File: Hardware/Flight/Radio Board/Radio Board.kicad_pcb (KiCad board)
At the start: 2 copper layers, 82 x 82 mm, 16 parts, among them J1 Conn_01x20_Female, J2 Conn_Coaxial, J3 Conn_Coaxial, U1 RFM95W-915S2, U2 RFM95W-915S2

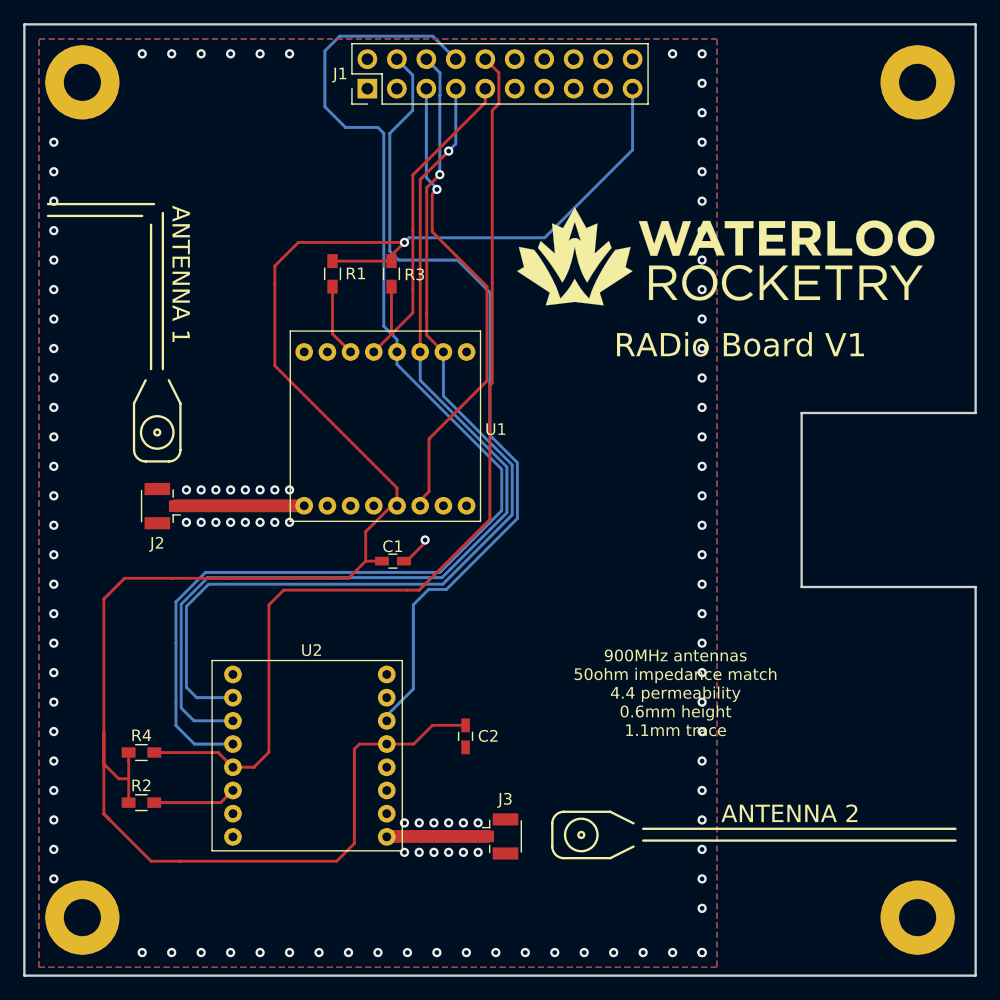
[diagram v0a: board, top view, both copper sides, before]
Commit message: Radio Review
Added Debug LEDs
Rerouted traces to keep away from edge
Made RF traces shorter
Switched RFM95W to SMD version
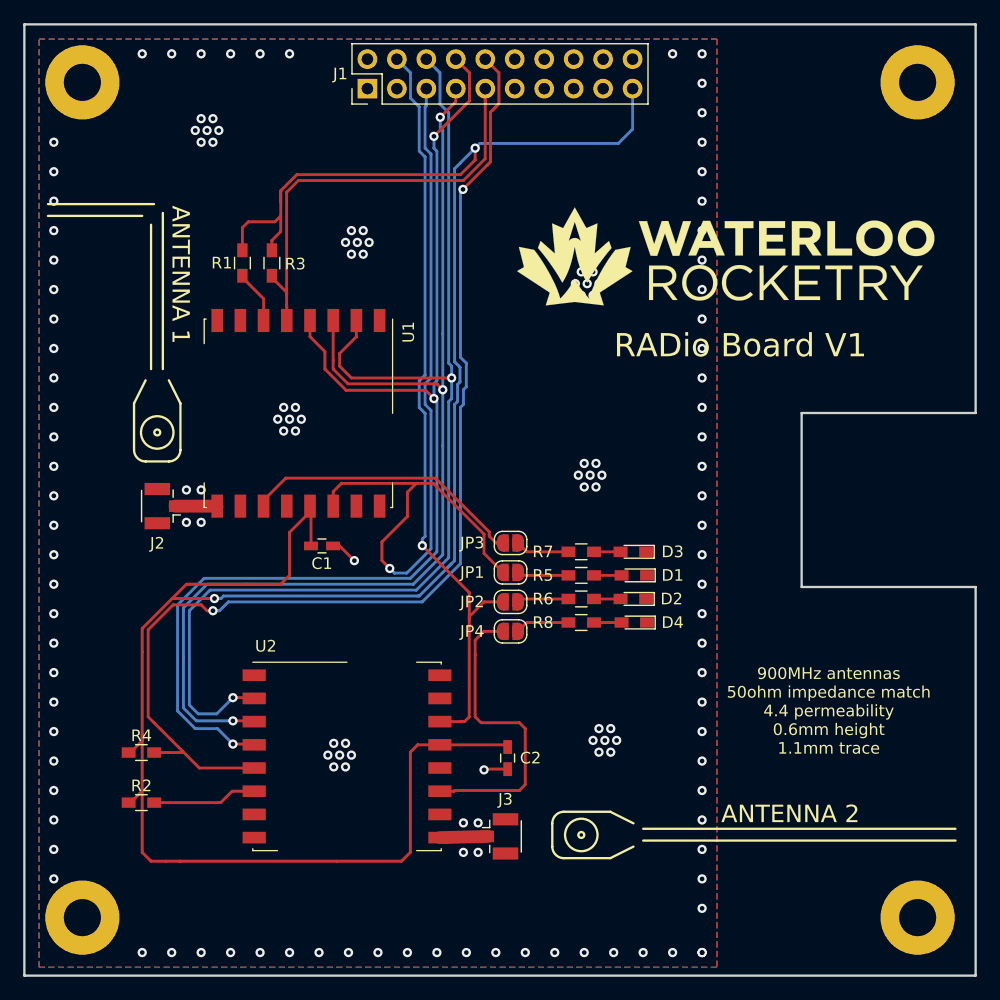
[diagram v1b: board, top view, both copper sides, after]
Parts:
- added D1: LED, LEDs:LED_0603_HandSoldering, F.Cu at (52.6, 47.5)
- added D2: LED, LEDs:LED_0603_HandSoldering, F.Cu at (52.5, 49.5)
- added D3: LED, LEDs:LED_0603_HandSoldering, F.Cu at (52.5, 45.5)
- added D4: LED, LEDs:LED_0603_HandSoldering, F.Cu at (52.6, 51.6)
- added JP1: Jumper, Jumper:SolderJumper-2_P1.3mm_Open_RoundedPad1.0x1.5mm, F.Cu at (41.9, 47.2)
- added JP2: Jumper, Jumper:SolderJumper-2_P1.3mm_Open_RoundedPad1.0x1.5mm, F.Cu at (41.9, 49.8)
- added JP3: Jumper, Jumper:SolderJumper-2_P1.3mm_Open_RoundedPad1.0x1.5mm, F.Cu at (41.9, 44.7)
- added JP4: Jumper, Jumper:SolderJumper-2_P1.3mm_Open_RoundedPad1.0x1.5mm, F.Cu at (41.9, 52.3)
- added R5: 70, Resistors_SMD:R_0603_HandSoldering, F.Cu at (48.0, 47.5)
- added R6: 70, Resistors_SMD:R_0603_HandSoldering, F.Cu at (48.0, 49.5)
- added R7: 70, Resistors_SMD:R_0603_HandSoldering, F.Cu at (48.0, 45.5)
- added R8: 70, Resistors_SMD:R_0603_HandSoldering, F.Cu at (48.0, 51.6)
- U1, U2: footprint Payload_Radios:Hopref_RFM9XW_THT -> RF_Modules:Hopref_RFM9XW_SMD
- moved U1 15.4 mm to (23.6, 33.5)
- moved U2 12.1 mm to (27.8, 63.1)
- moved R3 10.4 mm to (21.3, 20.6)
- moved R1 7.82 mm to (18.8, 20.6)
- moved C1 6.26 mm to (25.7, 45.0)
- moved C2 4.08 mm to (41.7, 63.2)
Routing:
- net INT1: track 40.6 -> 74.6 mm
- net Net-(JP4-Pad1): track 0.00 -> 26.5 mm
- net +3V3: track 174.7 -> 200.8 mm, vias 1 -> 2
- net Net-(JP3-Pad1): track 0.00 -> 24.5 mm
- net CS2: track 86.3 -> 98.0 mm, vias 0 -> 2
- net MISO: track 86.1 -> 97.7 mm, vias 1 -> 2
- net MOSI: track 86.2 -> 94.9 mm, vias 1 -> 3
- net CS1: track 30.8 -> 38.8 mm
- net Net-(J2-Pad1): track 11.2 -> 3.68 mm
- net SCK: track 107.8 -> 100.9 mm, vias 0 -> 3
- net INT2: track 71.7 -> 66.5 mm, vias 0 -> 1
- net Net-(JP4-Pad2): track 0.00 -> 4.66 mm
- net Net-(JP3-Pad2): track 0.00 -> 4.66 mm
- net Net-(J3-Pad1): track 8.78 -> 4.19 mm
- net Net-(JP2-Pad2): track 0.00 -> 4.45 mm
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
